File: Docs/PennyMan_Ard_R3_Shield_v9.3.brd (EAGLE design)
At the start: 53.3 x 59.7 mm, 56 parts, among them J1 ARDUINO_R3_SHIELD, J2 618025211821, J4 1X4-BIG, U1 NUP4114NUP4114HMR6T1GTSOT-6, U2 TD62783AG, U3 FM24-SG, U4 74AHC1G125DBV, U5 NUP4114NUP4114HMR6T1GTSOT-6

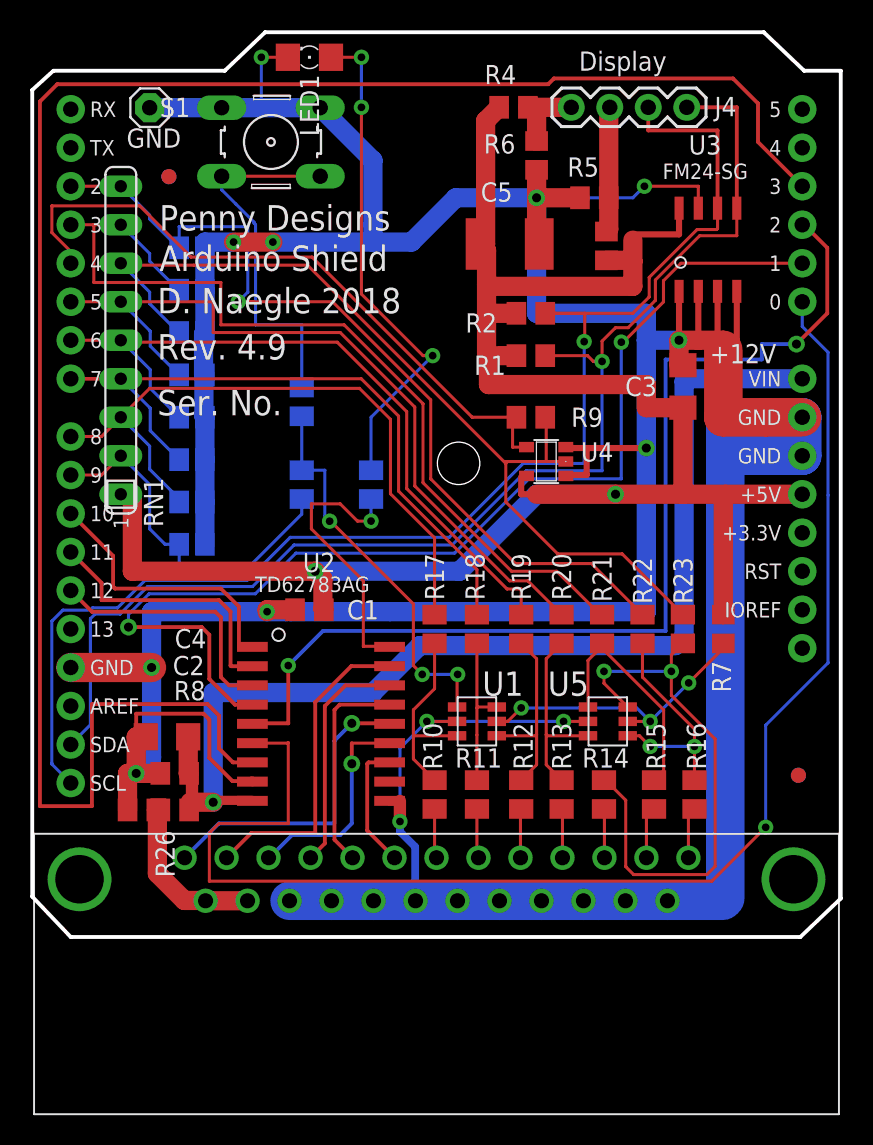
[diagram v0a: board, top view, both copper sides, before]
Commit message: Add files via upload
Older versions of schematic and layout files.  Note: earlier versions used the MAX chip for debouncing, but it never worked.
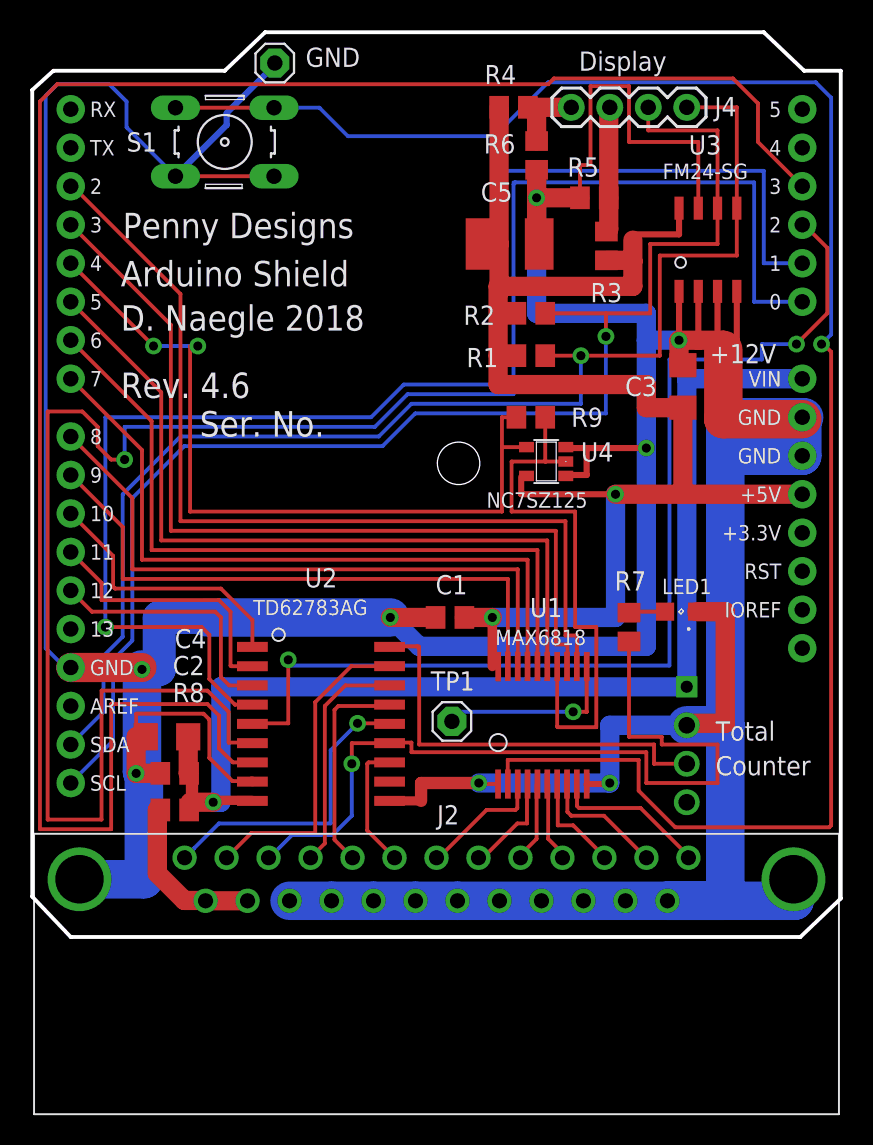
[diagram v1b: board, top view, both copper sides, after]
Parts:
- removed C10, C11, C12, C13, C6, C7, C8, C9: .01, adafruit:C0805
- removed R10, R11, R12, R13, R14, R15, R16, R25: 10, resistor:M0805
- removed R17, R18, R19, R20, R21, R22, R23, R24, R27: 1K, resistor:M0805
- removed R26: 0, resistor:R0805
- removed RN1: 10K, resistor-sil:SIL9
- removed U$1, U$2, U$3, U$4: FIDUCIAL, adafruit:FIDUCIAL_1MM
- removed U5: NUP4114NUP4114HMR6T1GTSOT-6, TSOT-23-6:TSOT-23-6
- added J3: TJC8-4P, NDN:TJC8-4P
- added TST1: TP1, adafruit:1X01
- LED1: device adafruit:1206 -> led:SML0805
- R1, R2: value 2K -> 10K
- R7: value 10K -> 1K
- U1: value NUP4114NUP4114HMR6T1GTSOT-6 -> MAX6818; device TSOT-23-6:TSOT-23-6 -> NDN:SSOP20
- moved LED1 44.0 mm to (42.7, 21.5)
- moved C1 9.28 mm to (27.4, 21.1)
- moved GND 8.77 mm to (15.9, 57.7)
- moved R7 6.22 mm to (39.2, 20.4), turned to 270 degrees
- moved U1 4.33 mm to (33.5, 14.0), turned to 0 degrees
- moved S1 3.05 mm to (12.6, 52.5), turned to 0 degrees
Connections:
- removed net N$13: R25.1, S1.1, S1.2
- removed net N$39: J2.6, R11.1
- removed net N$42: J2.4, R13.1
- removed net N$44: J2.2, R15.1
- removed net N$46: J2.1, R16.1
- removed net N$48: J2.3, R14.1
- removed net N$50: J2.5, R12.1
- removed net N$52: J2.7, R10.1
- removed net N$53: C13.1, J1.D9, R24.2, RN1.2
- new net N$40: R9.1, U1.OUT6, U4.2
- net +12V: now also J3.P$1
- net +5V: now also U1.VCC; no longer R7.2, RN1.1
- net GND: now also J3.P$2, U1.EN_L, U1.GND; no longer C10.2, C11.2, C12.2, C13.2, C6.2, C7.2, C8.2, C9.2, R26.1, U1.2, U5.2
- net N$1: now also J2.1, U1.IN8; no longer C7.1, J1.D2, R22.2, RN1.9
- net N$10: now also J1.D7, U1.OUT3; no longer R11.2, R18.1, U1.6
- net N$11: now also J1.D6, U1.OUT4; no longer R12.2, R19.1, U1.4
- net N$12: now also J1.D5, U1.OUT5; no longer R13.2, R20.1, U5.3
- net N$14: now also J1.D3, U1.OUT7; no longer R14.2, R23.1, U5.6
- net N$15: now also J3.P$3, U2.18; no longer R7.1, U1.5, U5.5
- net N$16: now also J1.D2, U1.OUT8; no longer R15.2, R21.1, U5.1
- net N$2: now also J2.2, U1.IN7; no longer C8.1, J1.D3, R21.2, RN1.8
- net N$25: now also TST1.1, U1.CH_L; no longer R16.2, R22.1, U5.4
- net N$3: now also J2.3, U1.IN6; no longer C6.1, R23.2, R9.1, RN1.7, U4.2
- net N$33: now also LED1.A, R7.1; no longer R27.1, U2.18
- net N$34: now also R7.2
- net N$35: now also S1.1, S1.2, U1.IN1; no longer LED1.A, R27.2
- net N$38: no longer R26.2
- net N$4: now also J2.4, U1.IN5; no longer C9.1, J1.D5, R20.2, RN1.6
- net N$5: now also J2.5, U1.IN4; no longer C10.1, J1.D6, R19.2, RN1.5
- net N$6: now also J2.6, U1.IN3; no longer C11.1, J1.D7, R18.2, RN1.4
- net N$7: now also J2.7, U1.IN2; no longer C12.1, J1.D8, R17.2, RN1.3
- net N$8: now also J1.D9, U1.OUT1; no longer R24.1, R25.2, U1.1
- net N$9: now also J1.D8, U1.OUT2; no longer R10.2, R17.1, U1.3
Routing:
- net N$35: track 33.3 -> 120.6 mm, vias 3 -> 1
- net N$3: track 61.4 -> 6.75 mm
- net N$2: track 60.3 -> 8.31 mm
- net N$1: track 59.2 -> 10.3 mm, vias 1 -> 0
- net N$4: track 51.6 -> 5.28 mm
- net N$16: track 15.4 -> 60.9 mm
- net N$5: track 47.9 -> 5.32 mm
- net GND: track 339.4 -> 381.8 mm, vias 13 -> 8
- net N$6: track 48.1 -> 6.75 mm
- net N$12: track 12.6 -> 52.0 mm
- net N$34: track 14.2 -> 53.4 mm
- net N$17: track 91.6 -> 128.4 mm
- net N$11: track 12.5 -> 49.2 mm
- net N$7: track 44.5 -> 8.28 mm
- net N$40: track 0.00 -> 36.2 mm
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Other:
- board text added: "C1"
- board text added: "C2"
- board text added: "C3"
- board text added: "C4"
- board text added: "C5"
- board text added: "Counter"
- board text added: "J2"
- board text added: "LED1"
- board text added: "NC7SZ125"
- board text added: "R1"
- board text added: "R2"
- board text added: "R4"
- board text added: "R5"
- board text added: "R6"
- board text added: "R7"
- board text added: "R8"
- board text added: "R9"
- board text added: "Rev. 4.6"
- board text added: "Total"
- board text added: "U1"
- board text added: "U2"
- board text added: "U4"
- board text removed: "Rev. 4.9"
